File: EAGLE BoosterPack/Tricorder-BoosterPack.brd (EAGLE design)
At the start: 63.5 x 34.3 mm, 18 parts

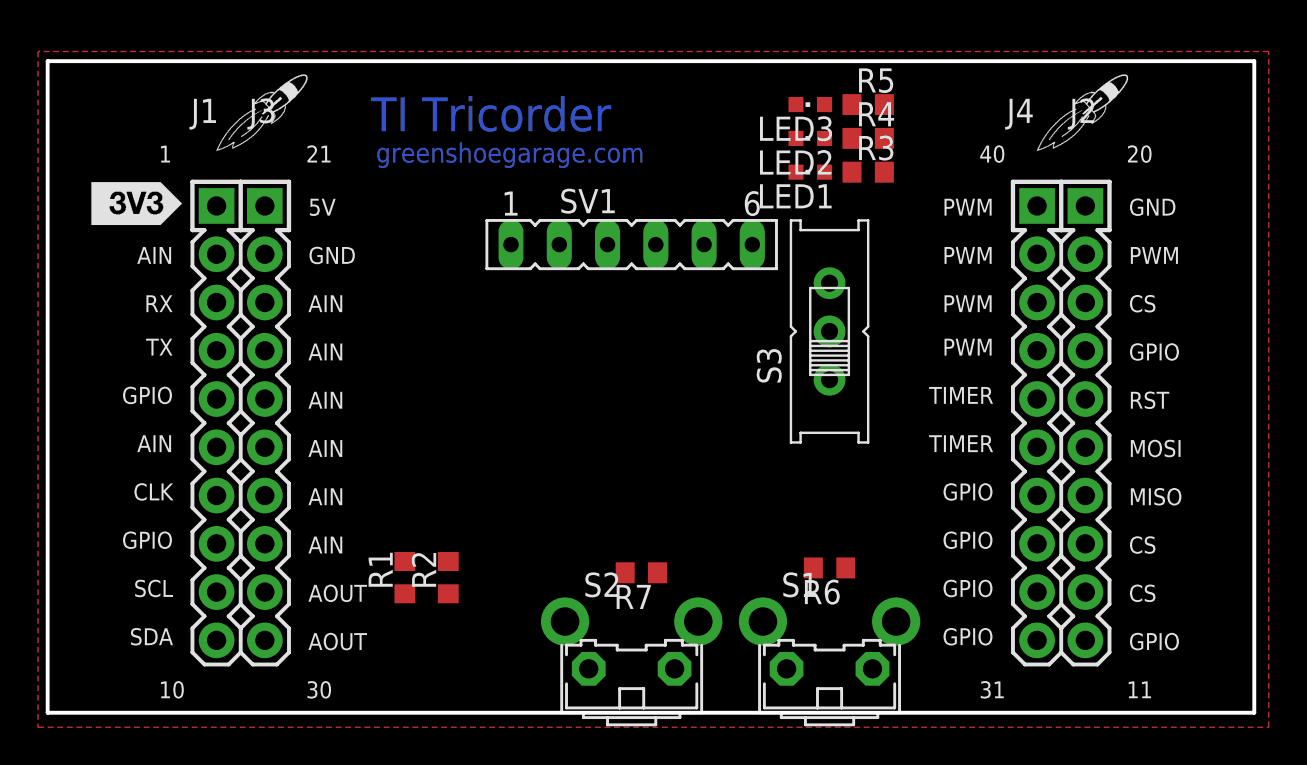
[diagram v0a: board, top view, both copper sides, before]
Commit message: SCH/BRD update, Init firmware
Added 4 main sensors to schematic and PMOD, buttons, LEDs, necessary
peripheral components.

Initial firmware release.
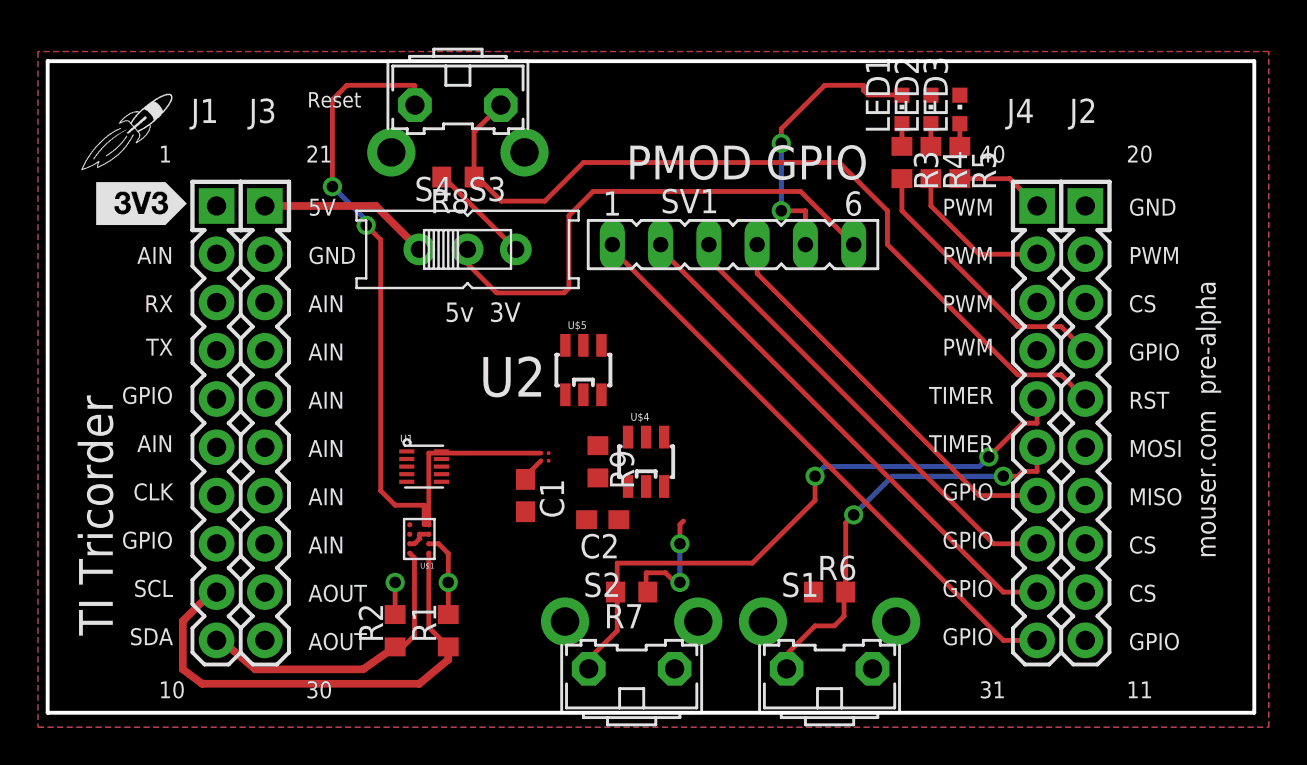
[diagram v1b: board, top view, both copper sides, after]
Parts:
- added C1: (no value), adafruit:C0603
- added C2: 0.1u, adafruit:C0603
- added R8: 47k, resistor:R0603
- added R9: 10k, resistor:R0603
- added S4: (no value), adafruit:EG1218
- added U$4: OPT3001, OPT3001:SOT23-6
- added U$5: TPL5010, LPT5010:TPL5010
- added U1: MAG3110, SparkFun-Sensors:DFN-10
- added U2: LMT70LMT70, LMT70:BGA4C40P2X2_77X77X50
- S3: device adafruit:EG1218 -> adafruit:B3F-31XX
- U$1: value (none) -> HDC1000; device CCo-Boost:LOGO-ROCKET -> Fra:DSBGA_8_YPA
- moved U$1 41.7 mm to (19.6, 9.14), turned to 180 degrees
- moved S3 22.3 mm to (21.6, 30.7), turned to 180 degrees
- moved LED3 7.88 mm to (48.0, 31.8), turned to 0 degrees
- moved U$2 7.18 mm to (4.32, 30.7)
- moved LED2 6.53 mm to (46.5, 31.8), turned to 0 degrees
- moved LED1 5.85 mm to (45.0, 31.8), turned to 0 degrees
- moved R5 5.71 mm to (48.0, 29.0), turned to 270 degrees
- moved SV1 5.33 mm to (36.1, 24.6)
- moved R2 3.95 mm to (18.3, 4.32)
- moved R1 3.61 mm to (21.1, 4.32)
- moved R4 3.54 mm to (46.5, 29.0), turned to 270 degrees
- moved R3 1.85 mm to (45.0, 29.0), turned to 270 degrees
- moved R6 1.27 mm to (41.1, 6.35), turned to 0 degrees
- moved R7 1.14 mm to (30.7, 6.35)
- moved U$3 0.25 mm to (2.54, 25.7)
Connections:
- new net N$5: R9.1, U$4.5
- new net N$6: U2.A2
- net 3V: now also C2.1, R8.2, R9.2, S4.S, U$1.B1, U$4.1; no longer S3.S
- net 5V: now also S4.O; no longer S3.O
- net GND: now also C1.2, C2.2, S3.2, U$1.B2, U$1.C1, U$1.D1, U$4.2, U$4.3, U$5.2, U2.A1
- net LMT_TAO: now also C1.1, U2.B1
- net LMT_TON: now also U2.B2
- net N$4: now also S4.P; no longer S3.P
- net RST: now also R8.1, S3.1
- net SCL: now also U$1.A1, U$4.4, U1.7
- net SDA: now also U$1.A2, U$4.6, U1.6
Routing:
- net GND: track 0.00 -> 63.7 mm, vias 0 -> 6
- net RST: track 0.00 -> 44.1 mm
- net BTN1: track 0.00 -> 33.5 mm, vias 0 -> 2
- net IO1: track 0.00 -> 31.1 mm
- net IO2: track 0.00 -> 27.5 mm
- net N$4: track 0.00 -> 27.3 mm
- net SCL: track 0.00 -> 25.7 mm
- net IO3: track 0.00 -> 24.2 mm
- net BTN0: track 0.00 -> 22.0 mm, vias 0 -> 2
- net IO4: track 0.00 -> 21.1 mm
- net SDA: track 0.00 -> 16.0 mm
- net LED0: track 0.00 -> 14.4 mm
- net 3V: track 0.00 -> 11.7 mm, vias 0 -> 2
- net 5V: track 0.00 -> 9.07 mm
- net LED1: track 0.00 -> 8.08 mm
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- added copper zone on layer 16, net 3V
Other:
- board text added: "5v 3V"
- board text added: "PMOD GPIO"
- board text added: "Reset"
- board text added: "mouser.com pre-alpha"
- board text removed: "greenshoegarage.com"
